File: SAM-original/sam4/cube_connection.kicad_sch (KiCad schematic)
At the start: 1 part

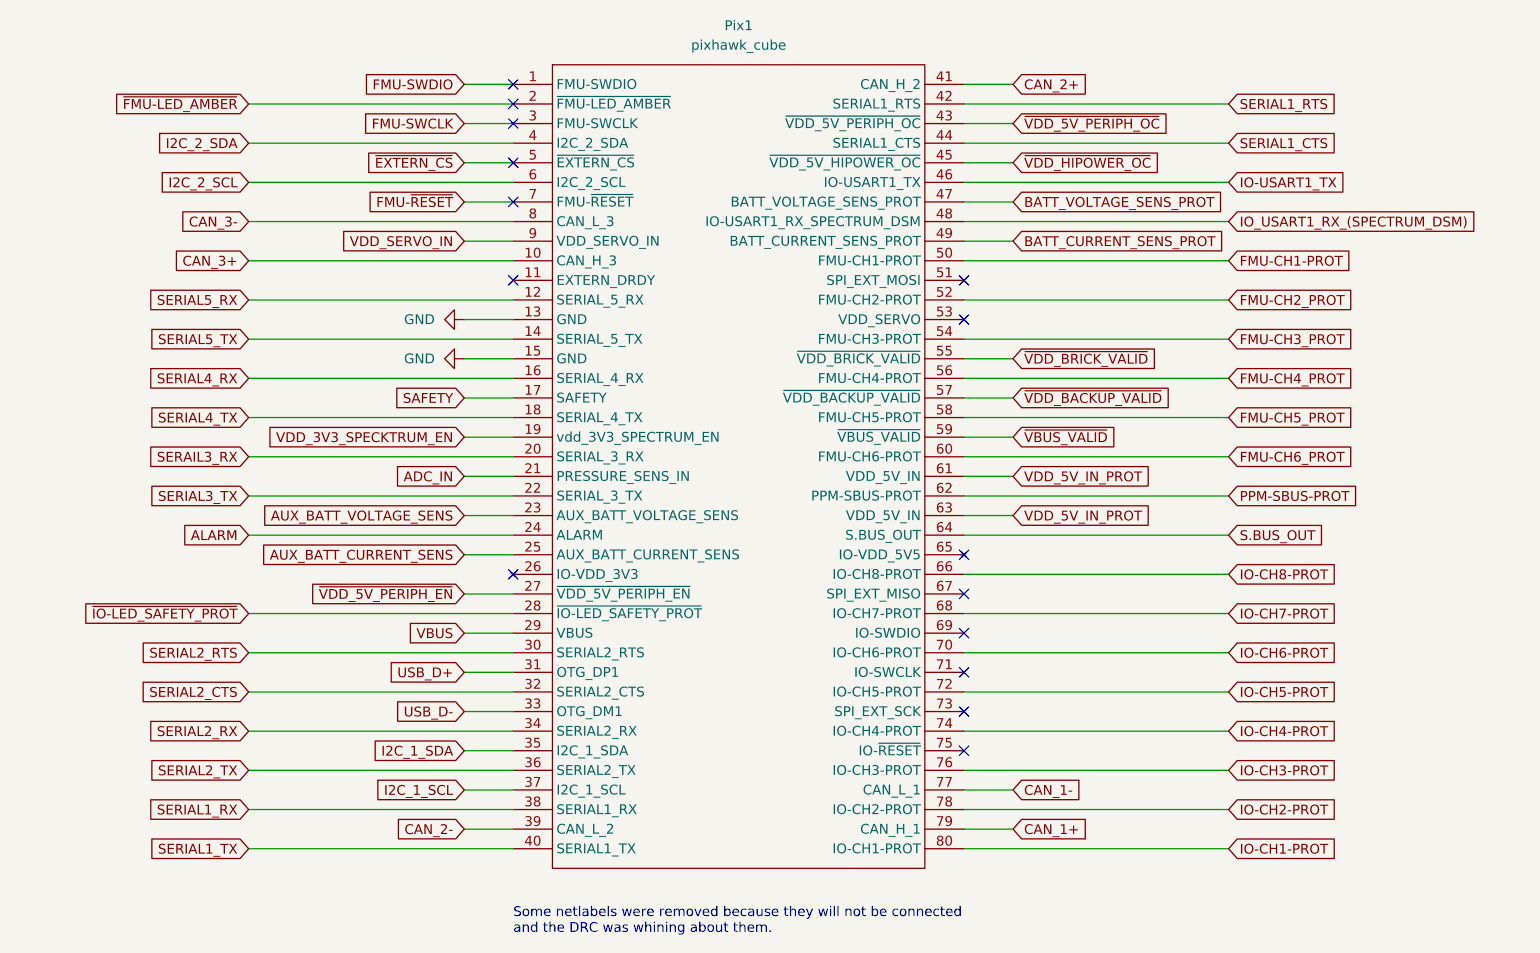
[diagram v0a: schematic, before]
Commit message: add updated SAM4 routing (DRC clean) + model
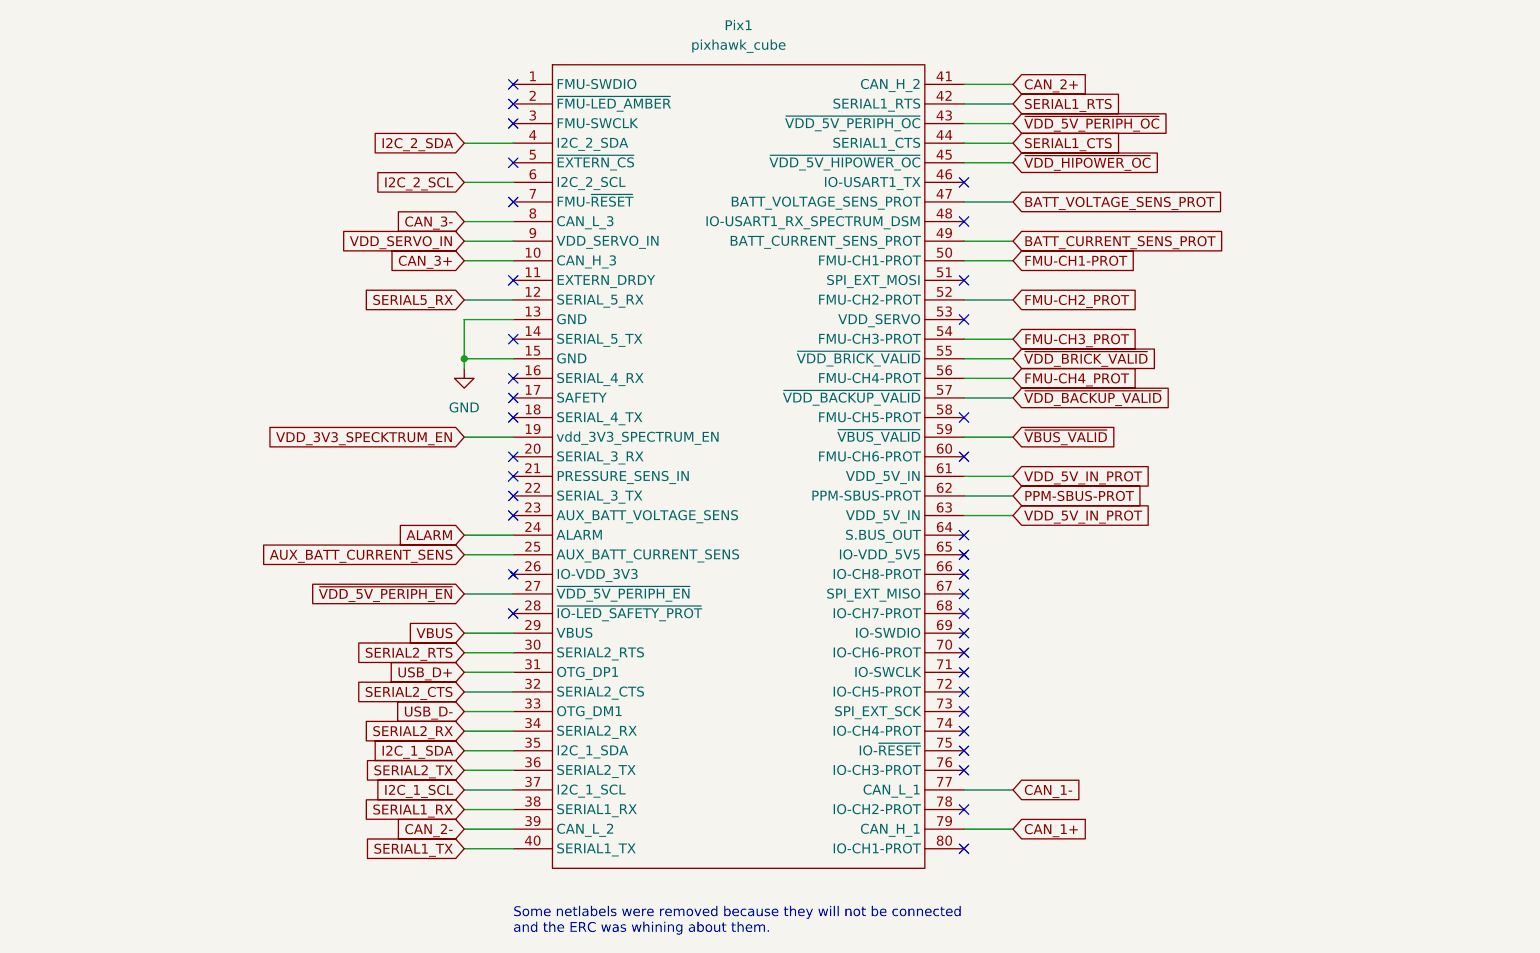
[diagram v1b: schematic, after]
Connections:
- net ADC_IN: no longer names the net of Pix1.21 (PRESSURE_SENS_IN)
- net AUX_BATT_VOLTAGE_SENS: no longer names the net of Pix1.23 (AUX_BATT_VOLTAGE_SENS)
- net FMU-CH5_PROT: no longer names the net of Pix1.58 (FMU-CH5-PROT)
- net FMU-CH6_PROT: no longer names the net of Pix1.60 (FMU-CH6-PROT)
- net FMU-SWCLK: no longer names the net of Pix1.3 (FMU-SWCLK)
- net FMU-SWDIO: no longer names the net of Pix1.1 (FMU-SWDIO)
- net FMU-~{RESET}: no longer names the net of Pix1.7 (FMU-~{RESET})
- net IO-CH1-PROT: no longer names the net of Pix1.80 (IO-CH1-PROT)
- net IO-CH2-PROT: no longer names the net of Pix1.78 (IO-CH2-PROT)
- net IO-CH3-PROT: no longer names the net of Pix1.76 (IO-CH3-PROT)
- net IO-CH4-PROT: no longer names the net of Pix1.74 (IO-CH4-PROT)
- net IO-CH5-PROT: no longer names the net of Pix1.72 (IO-CH5-PROT)
- net IO-CH6-PROT: no longer names the net of Pix1.70 (IO-CH6-PROT)
- net IO-CH7-PROT: no longer names the net of Pix1.68 (IO-CH7-PROT)
- net IO-CH8-PROT: no longer names the net of Pix1.66 (IO-CH8-PROT)
- net IO-USART1_TX: no longer names the net of Pix1.46 (IO-USART1_TX)
- net IO_USART1_RX_(SPECTRUM_DSM): no longer names the net of Pix1.48 (IO-USART1_RX_SPECTRUM_DSM)
- net S.BUS_OUT: no longer names the net of Pix1.64 (S.BUS_OUT)
- net SAFETY: no longer names the net of Pix1.17 (SAFETY)
- net SERAIL3_RX: no longer names the net of Pix1.20 (SERIAL_3_RX)
- net SERIAL3_TX: no longer names the net of Pix1.22 (SERIAL_3_TX)
- net SERIAL4_RX: no longer names the net of Pix1.16 (SERIAL_4_RX)
- net SERIAL4_TX: no longer names the net of Pix1.18 (SERIAL_4_TX)
- net SERIAL5_TX: no longer names the net of Pix1.14 (SERIAL_5_TX)
- net ~{EXTERN_CS}: no longer names the net of Pix1.5 (~{EXTERN_CS})
- net ~{FMU-LED_AMBER}: no longer names the net of Pix1.2 (~{FMU-LED_AMBER})
- net ~{IO-LED_SAFETY_PROT}: no longer names the net of Pix1.28 (~{IO-LED_SAFETY_PROT})
- no-connect marks 15 -> 37
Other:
- note added: "Some netlabels were removed because they will not be connected and the ERC was whining about them."
- note removed: "Some netlabels were removed because they will not be connected and the DRC was whining about them."
